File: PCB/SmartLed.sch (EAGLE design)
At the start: 49 parts, among them IC2 DS1307, IC3 MEGA8-P, K1 G5LE, Q2 32.768khz, T1 BC337

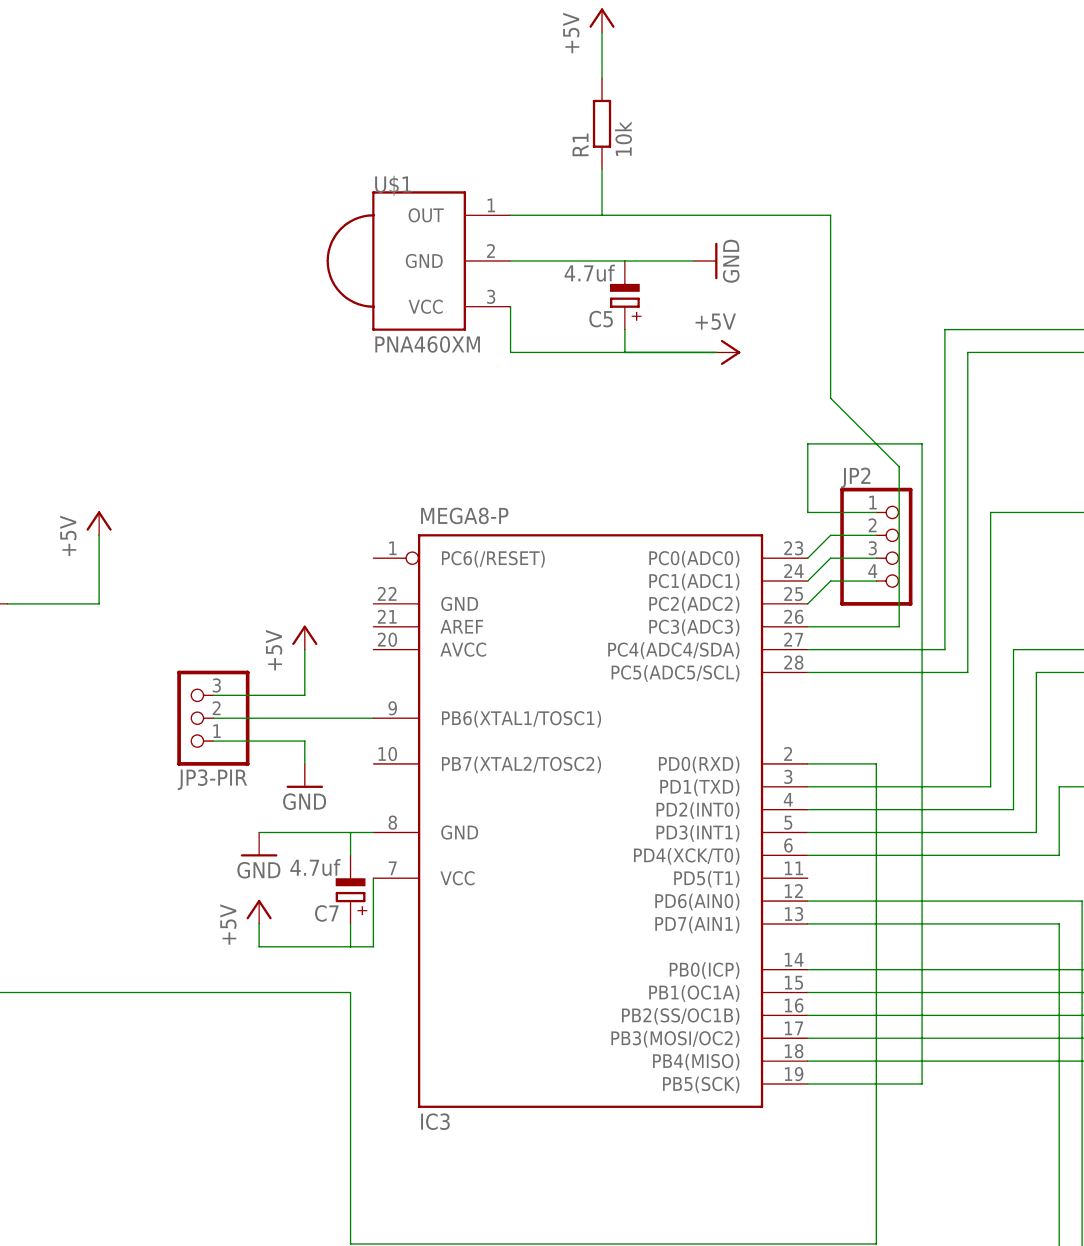
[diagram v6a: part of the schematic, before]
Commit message: Add a LDR off-board sensor
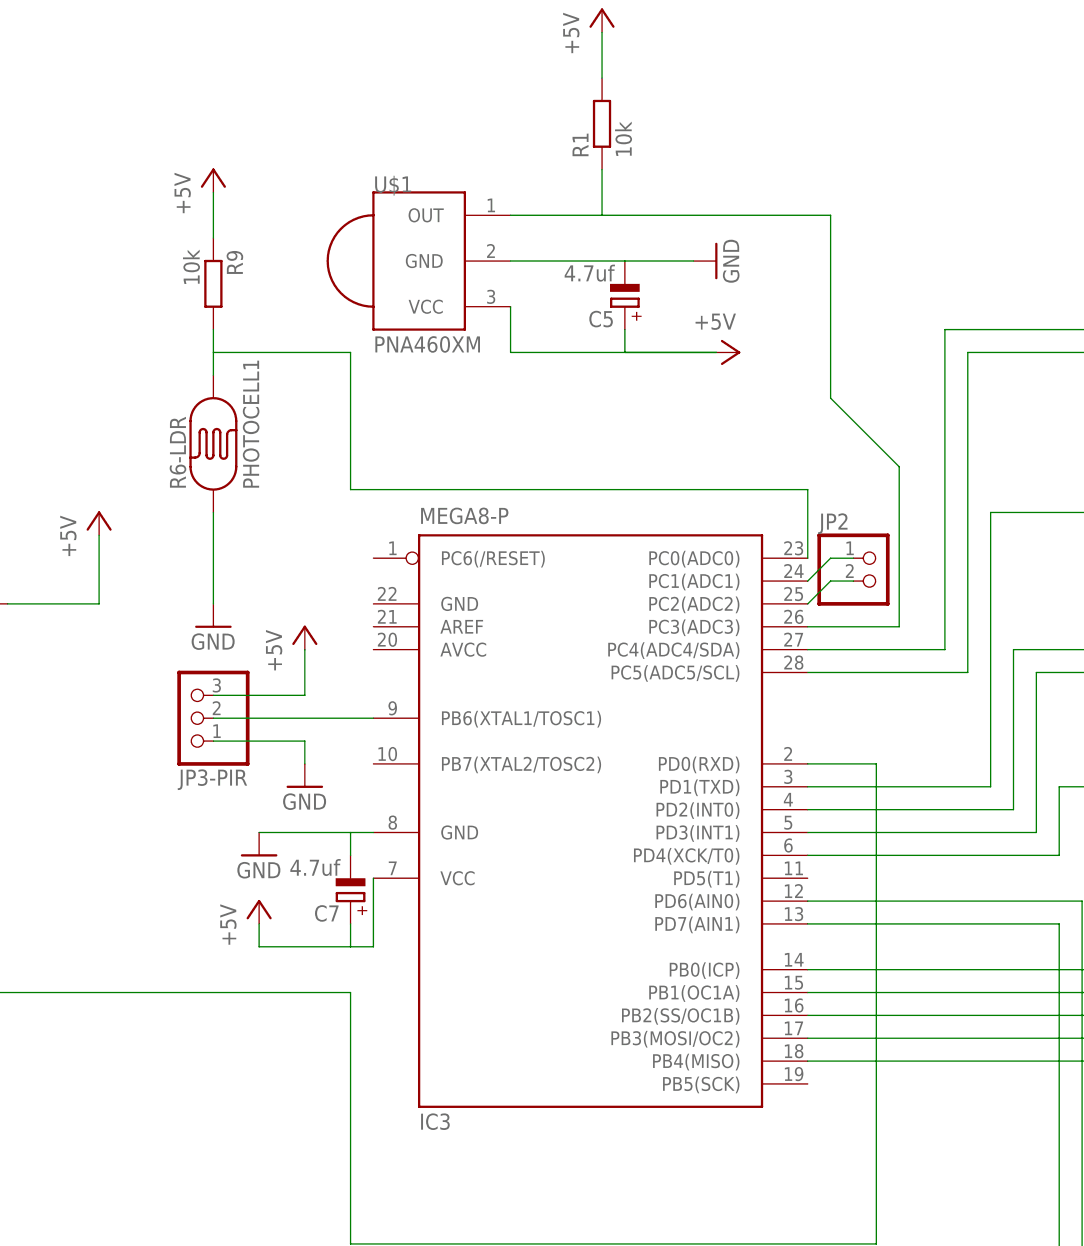
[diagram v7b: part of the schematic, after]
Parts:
- added R6-LDR: PHOTOCELL1, LDR:PHOTOCELL1
- added R9: 10k, rcl:R-EU_0207/10
- JP2: device pinhead:PINHD-1X4 -> pinhead:PINHD-1X2
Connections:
- removed net N$18: IC3.PC0(ADC0), JP2.2
- removed net N$40: IC3.PB5(SCK), JP2.1
- new net N$35: IC3.PC0(ADC0), R6-LDR.P$2, R9.2
- net +5V: now also R9.1
- net GND: now also R6-LDR.P$1
- net N$30: now also JP2.1; no longer JP2.3
- net N$34: now also JP2.2; no longer JP2.4
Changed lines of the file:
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@@
 <part name="GND16" library="supply1" deviceset="GND" device=""/>
 <part name="P+10" library="supply1" deviceset="+5V" device=""/>
-<part name="JP2" library="pinhead" deviceset="PINHD-1X4" device=""/>
 <part name="P+11" library="supply1" deviceset="+5V" device=""/>
 <part name="Q2" library="crystal" deviceset="CRYSTAL" device="TC26V" value="32.768khz"/>
@@
 <part name="P+13" library="supply1" deviceset="+5V" device=""/>
 <part name="IC1" library="v-reg" deviceset="78XXL" device=""/>
+<part name="R9" library="rcl" deviceset="R-EU_" device="0207/10" value="10k"/>
+<part name="P+14" library="supply1" deviceset="+5V" device=""/>
+<part name="GND19" library="supply1" deviceset="GND" device=""/>
+<part name="R6-LDR" library="LDR" deviceset="PHOTOCELL" device="1"/>
+<part name="JP2" library="pinhead" deviceset="PINHD-1X2" device=""/>
 </parts>
 <sheets>
@@
 <instance part="GND16" gate="1" x="81.28" y="149.86" rot="R90"/>
 <instance part="P+10" gate="1" x="83.82" y="139.7" rot="R270"/>
-<instance part="JP2" gate="A" x="101.6" y="116.84"/>
 <instance part="P+11" gate="1" x="68.58" y="177.8"/>
 <instance part="Q2" gate="G$1" x="182.88" y="154.94" rot="R90"/>
@@
 <instance part="P+13" gate="1" x="-81.28" y="99.06"/>
 <instance part="IC1" gate="A" x="-5.08" y="111.76"/>
+<instance part="R9" gate="G$1" x="25.4" y="147.32" rot="R270"/>
+<instance part="P+14" gate="1" x="25.4" y="160.02"/>
+<instance part="GND19" gate="1" x="25.4" y="109.22"/>
+<instance part="R6-LDR" gate="G$1" x="25.4" y="129.54" rot="R90"/>
+<instance part="JP2" gate="G$1" x="99.06" y="114.3"/>
 </instances>
 <busses>
@@
 <pinref part="JP3" gate="G$1" pin="1"/>
 <wire x1="-81.28" y1="91.44" x2="-71.12" y2="91.44" width="0.1524" layer="91"/>
+</segment>
+<segment>
+<pinref part="P+14" gate="1" pin="+5V"/>
+<pinref part="R9" gate="G$1" pin="1"/>
+<wire x1="25.4" y1="157.48" x2="25.4" y2="152.4" width="0.1524" layer="91"/>
 </segment>
 </net>
@@
 <wire x1="-81.28" y1="88.9" x2="-81.28" y2="81.28" width="0.1524" layer="91"/>
 </segment>
+<segment>
+<pinref part="R6-LDR" gate="G$1" pin="P$1"/>
+<wire x1="25.4" y1="121.92" x2="25.4" y2="111.76" width="0.1524" layer="91"/>
+<pinref part="GND19" gate="1" pin="GND"/>
+</segment>
 </net>
 <net name="N$12" class="0">
@@
 <pinref part="JP1" gate="G$1" pin="2"/>
 <wire x1="132.08" y1="35.56" x2="119.38" y2="35.56" width="0.1524" layer="91"/>
-</segment>
-</net>
-<net name="N$40" class="0">
-<segment>
-<pinref part="IC3" gate="G$1" pin="PB5(SCK)"/>
-<wire x1="91.44" y1="58.42" x2="104.14" y2="58.42" width="0.1524" layer="91"/>
-<wire x1="104.14" y1="58.42" x2="104.14" y2="129.54" width="0.1524" layer="91"/>
-<wire x1="104.14" y1="129.54" x2="91.44" y2="129.54" width="0.1524" layer="91"/>
-<wire x1="91.44" y1="129.54" x2="91.44" y2="121.92" width="0.1524" layer="91"/>
-<pinref part="JP2" gate="A" pin="1"/>
-<wire x1="99.06" y1="121.92" x2="91.44" y2="121.92" width="0.1524" layer="91"/>
 </segment>
 </net>
@@
 </segment>
 </net>
-<net name="N$18" class="0">
-<segment>
-<pinref part="JP2" gate="A" pin="2"/>
-<pinref part="IC3" gate="G$1" pin="PC0(ADC0)"/>
-<wire x1="99.06" y1="119.38" x2="93.98" y2="119.38" width="0.1524" layer="91"/>
-<wire x1="93.98" y1="119.38" x2="91.44" y2="116.84" width="0.1524" layer="91"/>
-</segment>
-</net>
 <net name="N$30" class="0">
 <segment>
-<pinref part="JP2" gate="A" pin="3"/>
 <pinref part="IC3" gate="G$1" pin="PC1(ADC1)"/>
-<wire x1="99.06" y1="116.84" x2="93.98" y2="116.84" width="0.1524" layer="91"/>
 <wire x1="93.98" y1="116.84" x2="91.44" y2="114.3" width="0.1524" layer="91"/>
+<pinref part="JP2" gate="G$1" pin="1"/>
+<wire x1="93.98" y1="116.84" x2="96.52" y2="116.84" width="0.1524" layer="91"/>
 </segment>
 </net>
 <net name="N$34" class="0">
 <segment>
-<pinref part="JP2" gate="A" pin="4"/>
 <pinref part="IC3" gate="G$1" pin="PC2(ADC2)"/>
-<wire x1="99.06" y1="114.3" x2="93.98" y2="114.3" width="0.1524" layer="91"/>
 <wire x1="93.98" y1="114.3" x2="91.44" y2="111.76" width="0.1524" layer="91"/>
+<pinref part="JP2" gate="G$1" pin="2"/>
+<wire x1="93.98" y1="114.3" x2="96.52" y2="114.3" width="0.1524" layer="91"/>
 </segment>
 </net>
@@
 </segment>
 </net>
+<net name="N$35" class="0">
+<segment>
+<pinref part="R9" gate="G$1" pin="2"/>
+<pinref part="R6-LDR" gate="G$1" pin="P$2"/>
+<wire x1="25.4" y1="142.24" x2="25.4" y2="139.7" width="0.1524" layer="91"/>
+<wire x1="25.4" y1="139.7" x2="25.4" y2="137.16" width="0.1524" layer="91"/>
+<wire x1="25.4" y1="139.7" x2="40.64" y2="139.7" width="0.1524" layer="91"/>
+<wire x1="40.64" y1="139.7" x2="40.64" y2="124.46" width="0.1524" layer="91"/>
+<wire x1="40.64" y1="124.46" x2="91.44" y2="124.46" width="0.1524" layer="91"/>
+<pinref part="IC3" gate="G$1" pin="PC0(ADC0)"/>
+<wire x1="91.44" y1="124.46" x2="91.44" y2="116.84" width="0.1524" layer="91"/>
+</segment>
+</net>

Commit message: Fix leds draining power from MCU I/O pins & make 12v lines thicker (after some problems caused by long time usge)
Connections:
- removed net N$29: LED8.A, R13.2
- new net N$18: LED8.A, R13.1
- net +5V: now also R10.2, R11.2, R12.2, R13.2
- net GND: no longer LED5.C, LED6.C, LED7.C, LED8.C
- net N$17: now also LED8.C; no longer R13.1
- net N$20: now also LED7.C; no longer R12.1
- net N$23: now also LED7.A, R12.1; no longer LED5.A, R10.2
- net N$24: now also LED6.C; no longer R11.1
- net N$25: now also R11.1; no longer R11.2
- net N$26: now also LED5.C; no longer R10.1
- net N$27: now also LED5.A, R10.1; no longer LED7.A, R12.2
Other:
- moved on the sheet: R10, R11, R12, R13
